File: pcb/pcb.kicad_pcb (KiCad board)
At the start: 2 copper layers, 120 x 90 mm, 92 parts, among them J301 USB_C_Receptacle_USB2.0_16P, Q201 IRL540N, Q301 Q_Dual_PMOS_S1G1S2G2D2D2D1D1, T201 >VALUE, U1 K155ID1, U2 K155ID1, U201 LM5155, U3 K155ID1, U301 CYPD3176, U4 K155ID1, U401 AP63205WU, U411 AP63203WU

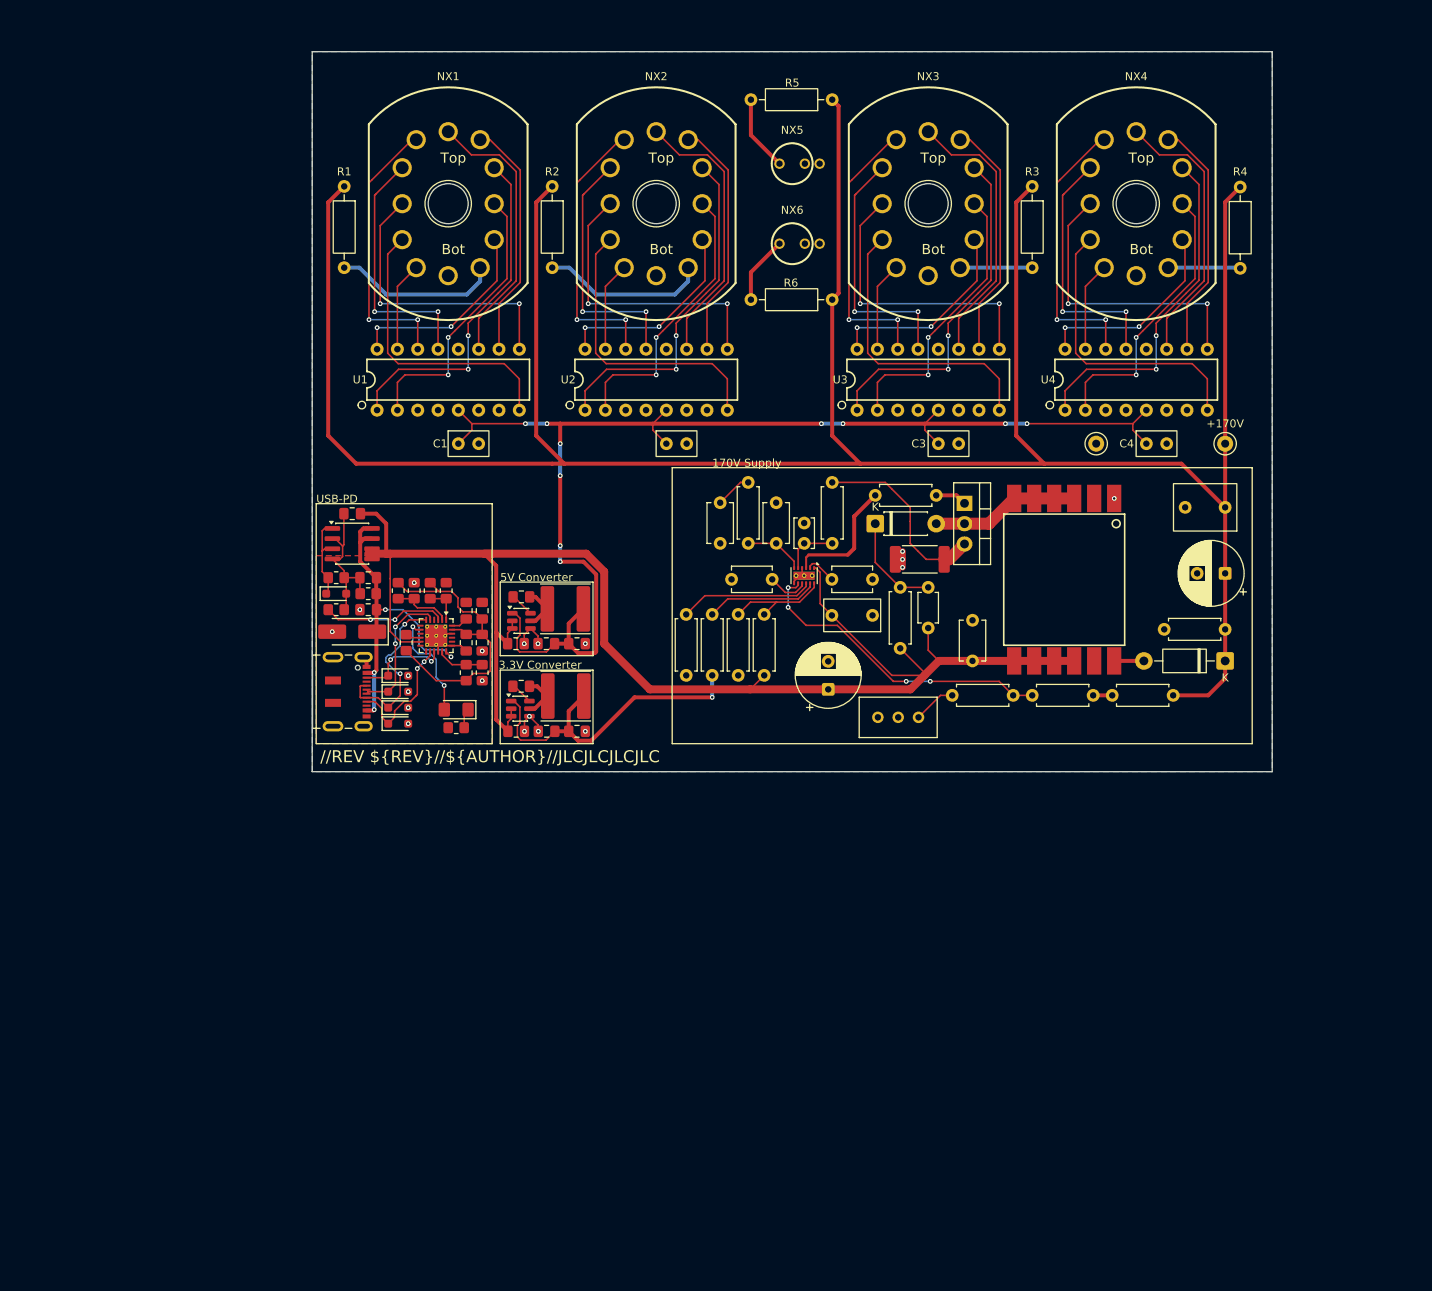
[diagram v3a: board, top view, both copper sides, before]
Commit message: Add ESP32, finish wiring. Rev A complete
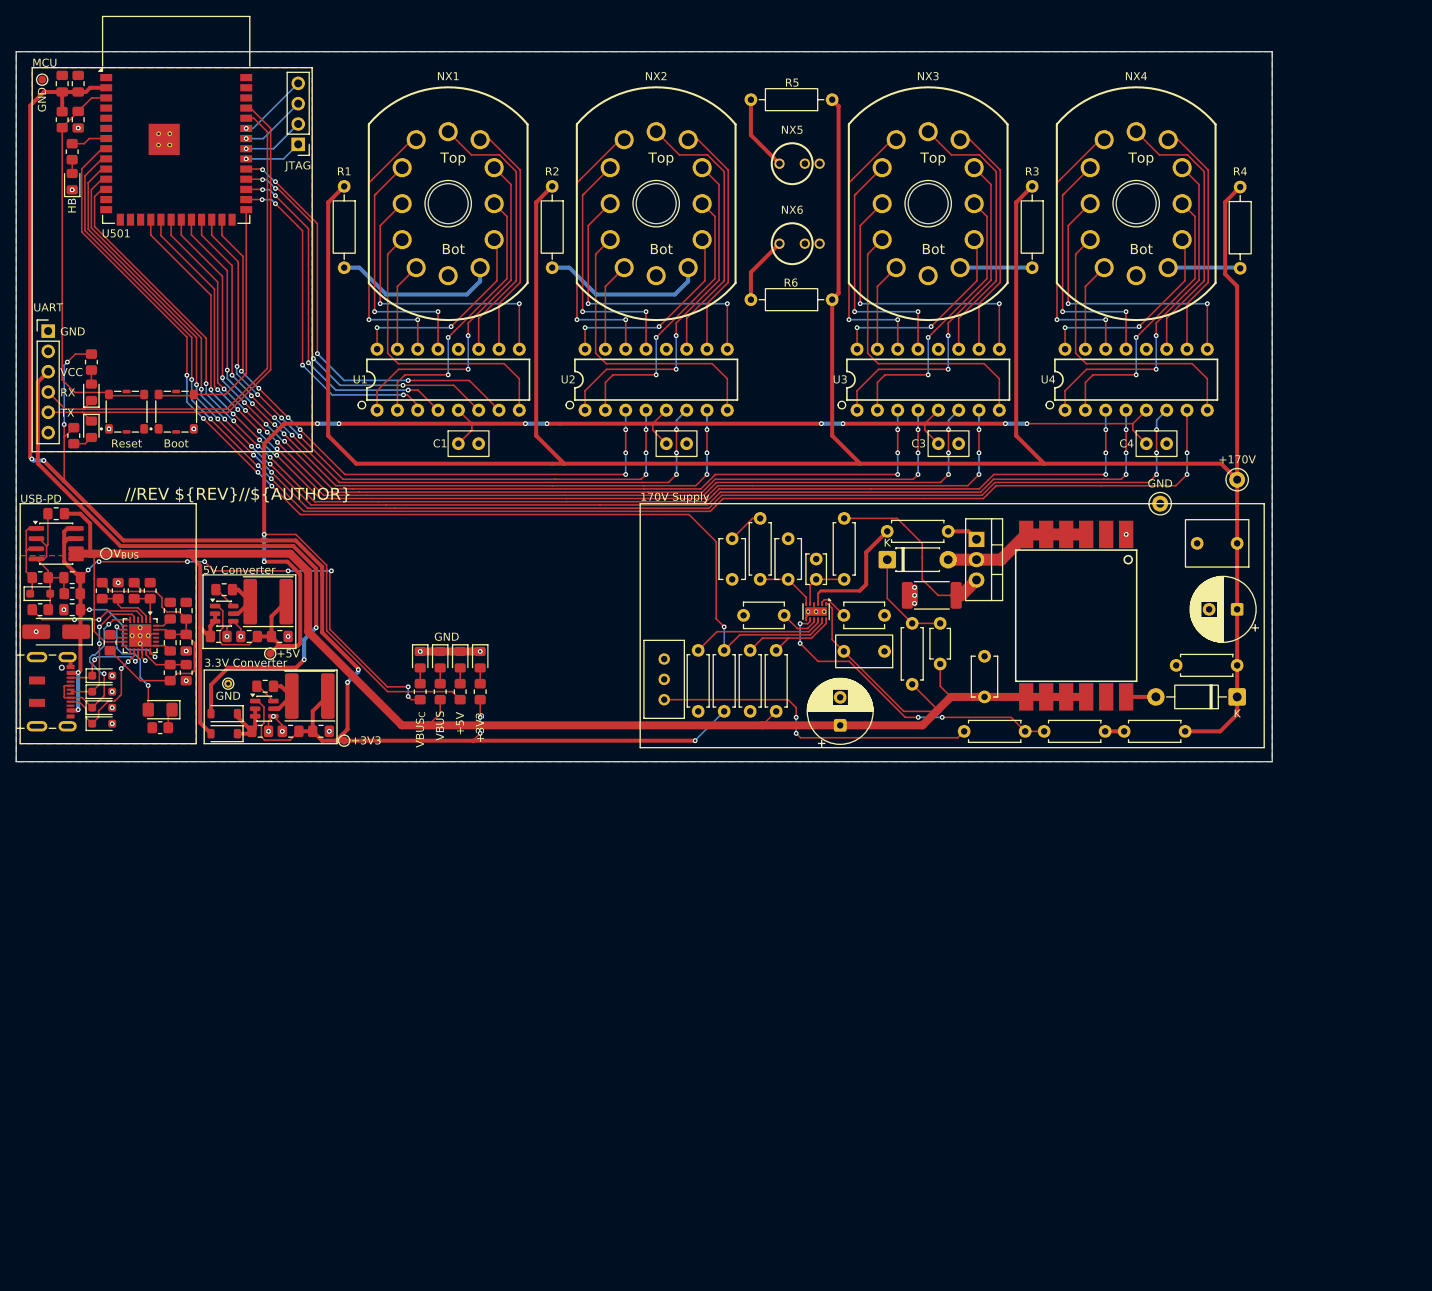
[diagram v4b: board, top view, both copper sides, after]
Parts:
- added C501: 100nF, Capacitor_SMD:C_0805_2012Metric_Pad1.18x1.45mm_HandSolder, F.Cu at (32.8, 43.0)
- added C502: 22uF, Capacitor_SMD:C_0805_2012Metric_Pad1.18x1.45mm_HandSolder, F.Cu at (30.8, 43.0)
- added C503: 1uF, Capacitor_SMD:C_0805_2012Metric_Pad1.18x1.45mm_HandSolder, F.Cu at (32.8, 47.5)
- added D301: VBUS_{C}, LED_SMD:LED_0805_2012Metric_Pad1.15x1.40mm_HandSolder, F.Cu at (75.5, 115.0)
- added D309: VBUS, LED_SMD:LED_0805_2012Metric_Pad1.15x1.40mm_HandSolder, F.Cu at (78.0, 115.0)
- added D310: HB, LED_SMD:LED_0805_2012Metric_Pad1.15x1.40mm_HandSolder, F.Cu at (32.0, 55.2)
- added D401: +5V, LED_SMD:LED_0805_2012Metric_Pad1.15x1.40mm_HandSolder, F.Cu at (80.5, 115.0)
- added D411: D_Schottky, Diode_SMD:D_SOD-123, F.Cu at (51.0, 124.2)
- added D412: D_Schottky, Diode_SMD:D_SOD-123, F.Cu at (51.0, 121.8)
- added D413: +3V3, LED_SMD:LED_0805_2012Metric_Pad1.15x1.40mm_HandSolder, F.Cu at (83.0, 115.0)
- added D501: TX, LED_SMD:LED_0805_2012Metric_Pad1.15x1.40mm_HandSolder, F.Cu at (34.4, 81.6)
- added D502: RX, LED_SMD:LED_0805_2012Metric_Pad1.15x1.40mm_HandSolder, F.Cu at (34.4, 86.2)
- added J302: JTAG, Connector_PinHeader_2.54mm:PinHeader_1x04_P2.54mm_Vertical, F.Cu at (60.2, 50.6)
- added J501: UART, Connector_PinHeader_2.54mm:PinHeader_1x06_P2.54mm_Vertical, F.Cu at (29.0, 73.9)
- added R301: 5.1k, Resistor_SMD:R_0805_2012Metric_Pad1.20x1.40mm_HandSolder, F.Cu at (75.5, 119.0)
- added R312: 10k, Resistor_SMD:R_0805_2012Metric_Pad1.20x1.40mm_HandSolder, F.Cu at (78.0, 119.0)
- added R314: 1.5k, Resistor_SMD:R_0805_2012Metric_Pad1.20x1.40mm_HandSolder, F.Cu at (32.0, 51.5)
- added R401: 5.1k, Resistor_SMD:R_0805_2012Metric_Pad1.20x1.40mm_HandSolder, F.Cu at (80.5, 119.0)
- added R411: 1.5k, Resistor_SMD:R_0805_2012Metric_Pad1.20x1.40mm_HandSolder, F.Cu at (83.0, 119.0)
- added R501: 10k, Resistor_SMD:R_0805_2012Metric_Pad1.20x1.40mm_HandSolder, F.Cu at (30.8, 47.5)
- added R502: 1.5k, Resistor_SMD:R_0805_2012Metric_Pad1.20x1.40mm_HandSolder, F.Cu at (34.4, 77.8)
- added R503: 1.5k, Resistor_SMD:R_0805_2012Metric_Pad1.20x1.40mm_HandSolder, F.Cu at (32.2, 87.0)
- added SW501: Reset, nixie_clock:SW_Panasonic_EVQ_4.9x4.9mm, F.Cu at (38.8, 84.0)
- added SW502: Boot, nixie_clock:SW_Panasonic_EVQ_4.9x4.9mm, F.Cu at (45.0, 84.0)
- added TP301: V_{BUS}, TestPoint:TestPoint_Pad_D1.0mm, F.Cu at (36.2, 101.8)
- added TP401: +5V, TestPoint:TestPoint_Pad_D1.0mm, F.Cu at (56.8, 114.2)
- added TP402: GND, TestPoint:TestPoint_THTPad_D1.0mm_Drill0.5mm, F.Cu at (51.5, 118.0)
- added TP411: +3V3, TestPoint:TestPoint_Pad_D1.0mm, F.Cu at (66.0, 125.1)
- added TP501: GND, TestPoint:TestPoint_Pad_D1.0mm, F.Cu at (28.2, 42.5)
- added U501: ESP32-S3-WROOM-1, nixie_clock:ESP32-S3-WROOM-1, F.Cu at (45.0, 47.5)
- T201: value >VALUE -> DA2032-AL
- moved C401 37.2 mm to (50.3, 112.1)
- moved C402 37.2 mm to (51.0, 106.2)
- moved C403 37.2 mm to (54.1, 112.1)
- moved L401 37.2 mm to (56.5, 107.8)
- moved U401 37.2 mm to (51.0, 109.2)
- moved C404 37.2 mm to (58.0, 112.1)
- moved C301 37.0 mm to (32.0, 108.8)
- moved C302 37.0 mm to (44.2, 108.9)
- moved C303 37.0 mm to (32.0, 104.8)
- moved C304 37.0 mm to (46.2, 108.9)
- moved C305 37.0 mm to (46.2, 112.9)
- moved C306 37.0 mm to (30.0, 96.8)
- moved C307 37.0 mm to (44.2, 112.9)
- moved D302 37.0 mm to (35.8, 119.0)
- moved D303 37.0 mm to (35.8, 121.0)
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- renumbered C302 to C301, C301 to C302, C306 to C303, C305 to C304, C304 to C305, C307 to C306, C303 to C307, D301 to D302, D302 to D303, D303 to D304, D304 to D306, D306 to D307, D307 to D308, R308 to R302, R305 to R303, R306 to R304, R309 to R305, R310 to R306, R303 to R307, R304 to R308, R301 to R309, R302 to R310, R307 to R313
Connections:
- net /HV Supply/COMP renamed /HV/COMP
- net /HV Supply/CS renamed /HV/CS
- net /HV Supply/FB renamed /HV/FB
- net /HV Supply/GATE renamed /HV/GATE
- net /HV Supply/HV_{DIV} renamed /HV/HV_{DIV}
- net /HV Supply/HV_{SEC} renamed /HV/HV_{SEC}
- net /HV Supply/PGOOD renamed PGOOD_{LM5155}
- net /HV Supply/RT renamed /HV/RT
- net /HV Supply/SS renamed /HV/SS
- net /HV Supply/UVLO renamed /HV/UVLO
- net /HV Supply/VCC renamed /HV/VCC
- net /HV Supply/V_{SW} renamed /HV/V_{SW}
- net /Input Power/CC1 renamed /PWR/CC1
- net /Input Power/CC2 renamed /PWR/CC2
- net /Input Power/D+ renamed USB_{D+}
- net /Input Power/D- renamed USB_{D-}
- net /Input Power/FAULT renamed /PWR/FAULT
- net /Input Power/GATE renamed /PWR/GATE
- net /Input Power/SOURCE renamed /PWR/SOURCE
- net /Input Power/SW_{3.3V} renamed /PWR/SW_{3.3V}
- net /Input Power/SW_{5V} renamed /PWR/SW_{5V}
- net /Input Power/VBUS_{C} renamed /PWR/VBUS_{C}
- C411 pad 1: V_{BUS} -> Net-(D411-K)
- U411 pad 2: V_{BUS} -> Net-(D411-K)
- U411 pad 3: V_{BUS} -> Net-(D411-K)
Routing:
- net +3V3: track 41.1 -> 220.6 mm, vias 1 -> 9
- net M1_{C}: track 0.00 -> 177.2 mm, vias 0 -> 6
- net M1_{B}: track 0.00 -> 171.5 mm, vias 0 -> 7
- net M1_{D}: track 0.00 -> 164.7 mm, vias 0 -> 7
- net M1_{A}: track 0.00 -> 159.8 mm, vias 0 -> 7
- net M10_{C}: track 0.00 -> 135.4 mm, vias 0 -> 7
- net M10_{B}: track 0.00 -> 130.8 mm, vias 0 -> 7
- net PGOOD_{LM5155}: track 14.1 -> 140.2 mm, vias 0 -> 5
- net M10_{D}: track 0.00 -> 124.9 mm, vias 0 -> 7
- net M10_{A}: track 0.00 -> 121.0 mm, vias 0 -> 7
- net H1_{C}: track 0.00 -> 95.9 mm, vias 0 -> 7
- net H1_{B}: track 0.00 -> 91.2 mm, vias 0 -> 7
- net H1_{D}: track 0.00 -> 85.6 mm, vias 0 -> 7
- net H1_{A}: track 0.00 -> 81.5 mm, vias 0 -> 7
- net VCC_{UART}: track 0.00 -> 80.8 mm, vias 0 -> 2
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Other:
- board size 120 x 90 mm -> 157 x 88.8 mm
- board text added: "${TITLE}//REV ${REV}//${AUTHOR}"
- board text added: "Antenna"
- board text added: "GND"
- board text added: "MCU"
- board text added: "RX"
- board text added: "TX"
- board text added: "VCC"
- board text removed: "${TITLE}//REV ${REV}//${AUTHOR}//JLCJLCJLCJLC"
